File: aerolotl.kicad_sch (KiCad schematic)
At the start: 0 parts

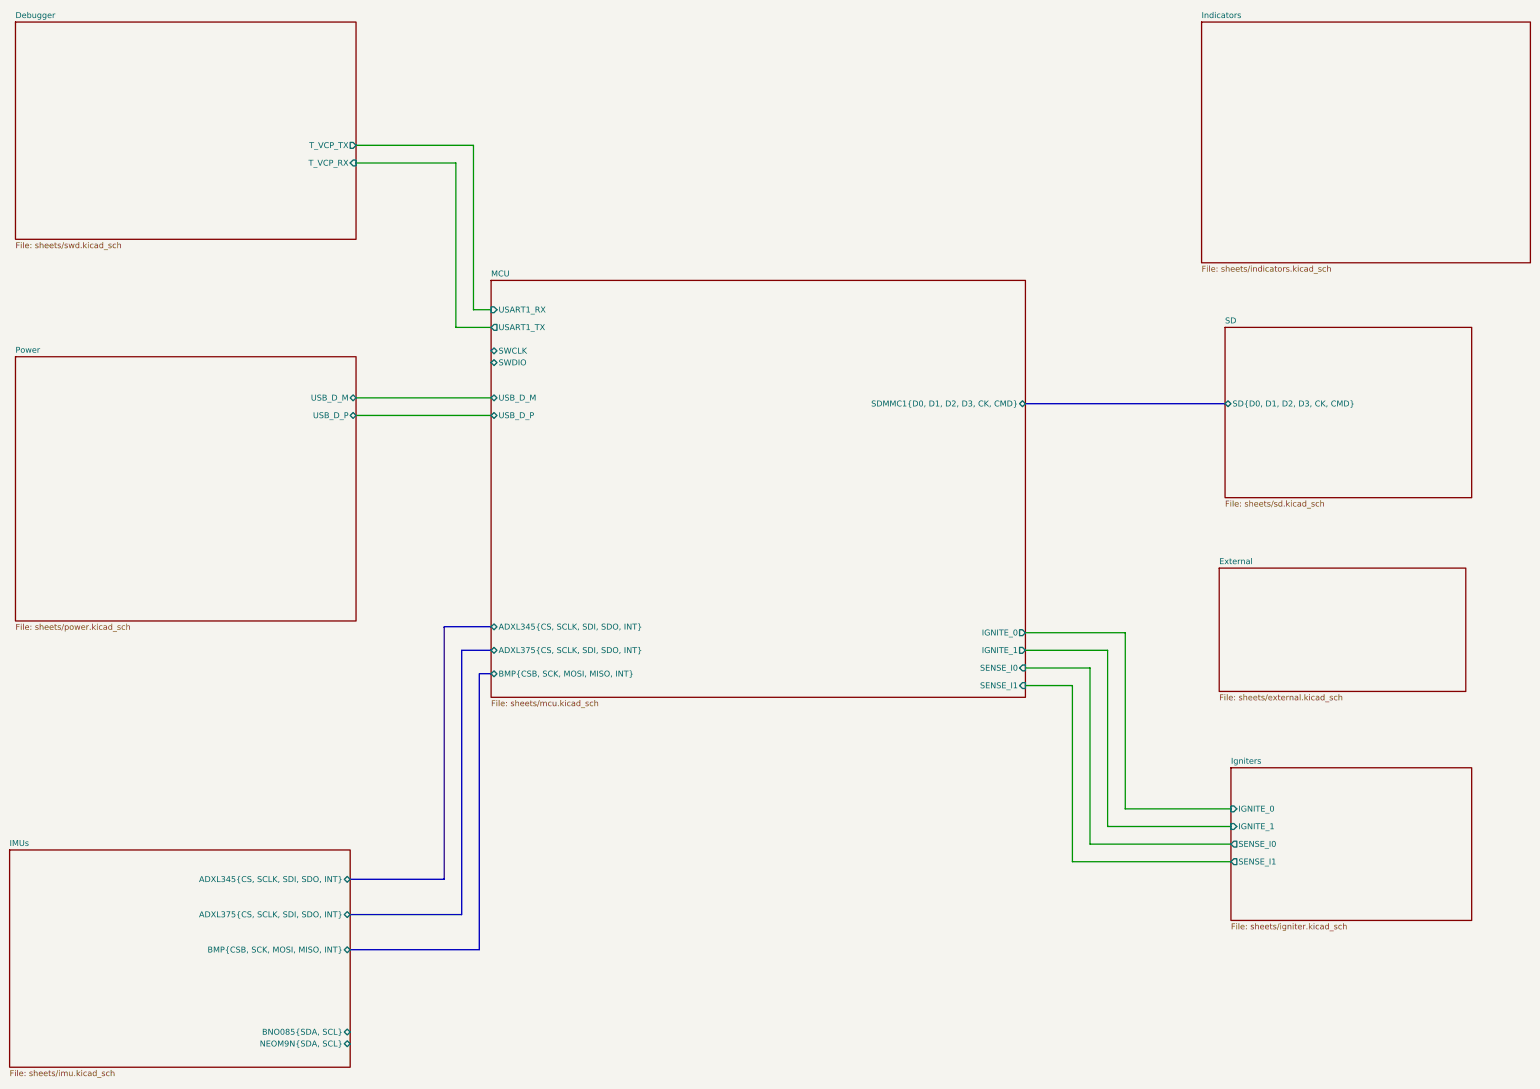
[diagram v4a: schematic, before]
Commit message: polished up circuit, added new 16.8V to 7.4V step down circuit components
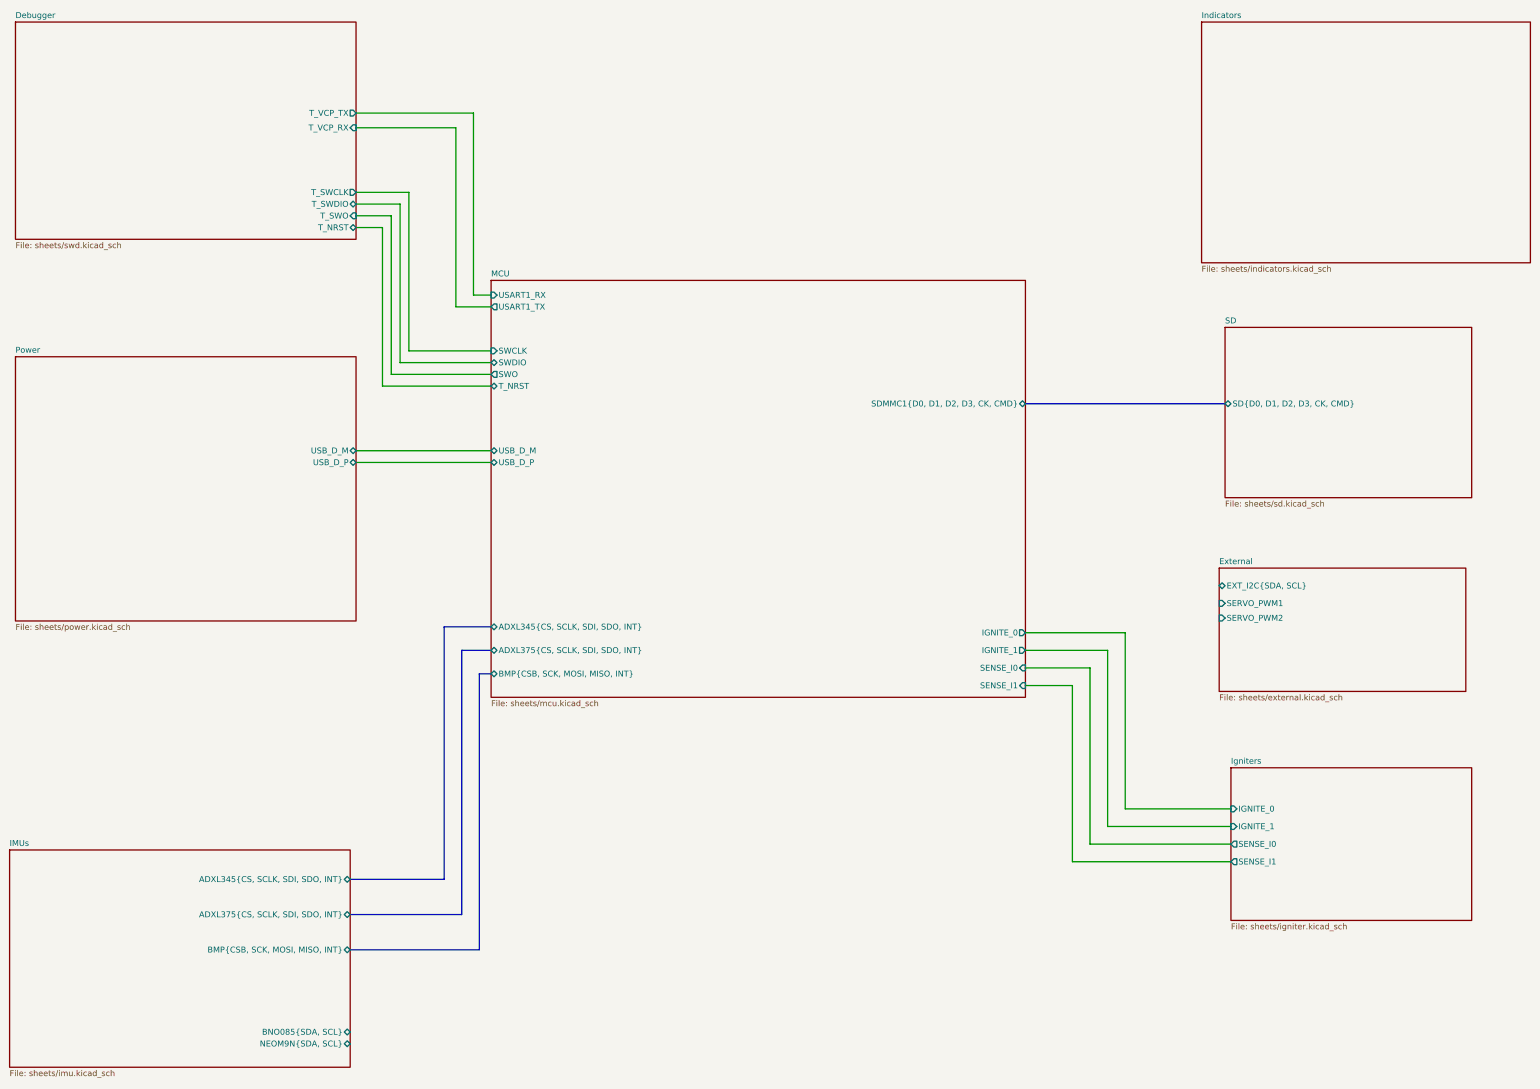
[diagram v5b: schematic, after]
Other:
- sheet Debugger ports: added T_NRST, T_SWCLK, T_SWDIO, T_SWO; removed none
- sheet External ports: added EXT_I2C{SDA, SCL}, SERVO_PWM1, SERVO_PWM2; removed none
- sheet MCU ports: added SWO, T_NRST; removed none
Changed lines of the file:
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@@
+	(wire
+		(pts
+			(xy 114.935 102.87) (xy 114.935 68.58)
+		)
+		(stroke
+			(width 0)
+			(type default)
+		)
+	)
 	(wire
 		(pts
@@
 	(wire
 		(pts
+			(xy 116.84 66.04) (xy 116.84 100.33)
+		)
+		(stroke
+			(width 0)
+			(type default)
+		)
+	)
+	(wire
+		(pts
+			(xy 105.41 71.12) (xy 113.03 71.12)
+		)
+		(stroke
+			(width 0)
+			(type default)
+		)
+	)
+	(wire
+		(pts
+			(xy 105.41 66.04) (xy 116.84 66.04)
+		)
+		(stroke
+			(width 0)
+			(type default)
+		)
+	)
+	(wire
+		(pts
 			(xy 250.19 161.29) (xy 271.78 161.29)
 		)
@@
 	(wire
 		(pts
-			(xy 105.41 59.69) (xy 127 59.69)
+			(xy 116.84 100.33) (xy 134.62 100.33)
+		)
+		(stroke
+			(width 0)
+			(type default)
+		)
+	)
+	(wire
+		(pts
+			(xy 105.41 52.07) (xy 127 52.07)
+		)
+		(stroke
+			(width 0)
+			(type default)
+		)
+	)
+	(wire
+		(pts
+			(xy 114.935 68.58) (xy 105.41 68.58)
+		)
+		(stroke
+			(width 0)
+			(type default)
+		)
+	)
+	(wire
+		(pts
+			(xy 134.62 102.87) (xy 114.935 102.87)
 		)
 		(stroke
@@
 	(wire
 		(pts
-			(xy 105.41 110.49) (xy 134.62 110.49)
+			(xy 113.03 71.12) (xy 113.03 105.41)
+		)
+		(stroke
+			(width 0)
+			(type default)
+		)
+	)
+	(wire
+		(pts
+			(xy 105.41 121.92) (xy 134.62 121.92)
 		)
 		(stroke
@@
 	(wire
 		(pts
+			(xy 113.03 105.41) (xy 134.62 105.41)
+		)
+		(stroke
+			(width 0)
+			(type default)
+		)
+	)
+	(wire
+		(pts
+			(xy 111.125 73.66) (xy 105.41 73.66)
+		)
+		(stroke
+			(width 0)
+			(type default)
+		)
+	)
+	(wire
+		(pts
+			(xy 111.125 107.95) (xy 111.125 73.66)
+		)
+		(stroke
+			(width 0)
+			(type default)
+		)
+	)
+	(wire
+		(pts
 			(xy 264.16 168.91) (xy 264.16 207.01)
 		)
@@
 	(wire
 		(pts
-			(xy 105.41 55.88) (xy 130.81 55.88)
+			(xy 105.41 48.895) (xy 130.81 48.895)
 		)
 		(stroke
@@
 	(wire
 		(pts
-			(xy 130.81 55.88) (xy 130.81 91.44)
+			(xy 130.81 48.895) (xy 130.81 88.265)
 		)
 		(stroke
@@
 	(wire
 		(pts
-			(xy 105.41 114.3) (xy 134.62 114.3)
-		)
-		(stroke
-			(width 0)
-			(type default)
-		)
-	)
-	(wire
-		(pts
-			(xy 130.81 91.44) (xy 134.62 91.44)
+			(xy 105.41 124.46) (xy 134.62 124.46)
+		)
+		(stroke
+			(width 0)
+			(type default)
+		)
+	)
+	(wire
+		(pts
+			(xy 130.81 88.265) (xy 134.62 88.265)
 		)
 		(stroke
@@
 	(wire
 		(pts
-			(xy 127 59.69) (xy 127 95.25)
-		)
-		(stroke
-			(width 0)
-			(type default)
-		)
-	)
-	(wire
-		(pts
-			(xy 127 95.25) (xy 134.62 95.25)
+			(xy 134.62 107.95) (xy 111.125 107.95)
+		)
+		(stroke
+			(width 0)
+			(type default)
+		)
+	)
+	(wire
+		(pts
+			(xy 127 52.07) (xy 127 90.805)
+		)
+		(stroke
+			(width 0)
+			(type default)
+		)
+	)
+	(wire
+		(pts
+			(xy 127 90.805) (xy 134.62 90.805)
 		)
 		(stroke
@@
 		)
 		(pin "T_VCP_RX" input
-			(at 105.41 59.69 0)
+			(at 105.41 52.07 0)
 			(effects
 				(font
@@
 		)
 		(pin "T_VCP_TX" output
-			(at 105.41 55.88 0)
+			(at 105.41 48.895 0)
+			(effects
+				(font
+					(size 1.27 1.27)
+				)
+				(justify right)
+			)
+		)
+		(pin "T_SWCLK" output
+			(at 105.41 66.04 0)
+			(effects
+				(font
+					(size 1.27 1.27)
+				)
+				(justify right)
+			)
+		)
+		(pin "T_SWDIO" bidirectional
+			(at 105.41 68.58 0)
+			(effects
+				(font
+					(size 1.27 1.27)
+				)
+				(justify right)
+			)
+		)
+		(pin "T_SWO" input
+			(at 105.41 71.12 0)
+			(effects
+				(font
+					(size 1.27 1.27)
+				)
+				(justify right)
+			)
+		)
+		(pin "T_NRST" bidirectional
+			(at 105.41 73.66 0)
 			(effects
 				(font
@@
 			)
 		)
+		(pin "EXT_I2C{SDA, SCL}" bidirectional
+			(at 292.1 151.13 180)
+			(effects
+				(font
+					(size 1.27 1.27)
+				)
+				(justify left)
+			)
+		)
+		(pin "SERVO_PWM1" input
+			(at 292.1 154.94 180)
+			(effects
+				(font
+					(size 1.27 1.27)
+				)
+				(justify left)
+			)
+		)
+		(pin "SERVO_PWM2" input
+			(at 292.1 158.115 180)
+			(effects
+				(font
+					(size 1.27 1.27)
+				)
+				(justify left)
+			)
+		)
 		(instances
 			(project "aerolotl"
@@
 		)
 		(pin "USB_D_M" bidirectional
-			(at 105.41 110.49 0)
+			(at 105.41 121.92 0)
 			(effects
 				(font
@@
 		)
 		(pin "USB_D_P" bidirectional
-			(at 105.41 114.3 0)
+			(at 105.41 124.46 0)
 			(effects
 				(font
@@
 		)
 		(pin "USART1_RX" input
-			(at 134.62 91.44 180)
+			(at 134.62 88.265 180)
 			(effects
 				(font
@@
 		)
 		(pin "USART1_TX" output
-			(at 134.62 95.25 180)
+			(at 134.62 90.805 180)
 			(effects
 				(font
@@
 			)
 		)
-		(pin "SWCLK" bidirectional
-			(at 134.62 100.33 180)
-			(effects
-				(font
-					(size 1.27 1.27)
-				)
-				(justify left)
-			)
-		)
 		(pin "SWDIO" bidirectional
 			(at 134.62 102.87 180)
@@
 		)
 		(pin "USB_D_M" bidirectional
-			(at 134.62 110.49 180)
+			(at 134.62 121.92 180)
 			(effects
 				(font
@@
 		)
 		(pin "USB_D_P" bidirectional
-			(at 134.62 114.3 180)
+			(at 134.62 124.46 180)
 			(effects
 				(font
@@
 			(effects
 				(font
+					(size 1.27 1.27)
+				)
+				(justify left)
+			)
+		)
+		(pin "SWCLK" input
+			(at 134.62 100.33 180)
+			(effects
+				(font
+					(size 1.27 1.27)
+				)
+				(justify left)
+			)
+		)
+		(pin "SWO" output
+			(at 134.62 105.41 180)
+			(effects
+				(font
+					(size 1.27 1.27)
+				)
+				(justify left)
+			)
+		)
+		(pin "T_NRST" bidirectional
+			(at 134.62 107.95 180)
+			(effects
+				(font

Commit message: second push
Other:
- sheet IMUs renamed Sensors
- sheet MCU ports: added NEOM9N_EXTI0, NEOM9N_RST, USART2_RX, USART2_TX; removed none
- sheet Sensors: file sheets/imu.kicad_sch -> sheets/sensors.kicad_sch
- sheet Sensors ports: added NEOM9N{TX, RX, PPS, RST}; removed NEOM9N{SDA, SCL}
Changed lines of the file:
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@@
 	(generator_version "9.0")
 	(paper "A3")
+	(bus_entry
+		(at 204.47 193.675)
+		(size 2.54 -2.54)
+		(stroke
+			(width 0)
+			(type default)
+		)
+	)
+	(bus_entry
+		(at 190.5 193.675)
+		(size 2.54 -2.54)
+		(stroke
+			(width 0)
+			(type default)
+		)
+	)
+	(bus_entry
+		(at 200.025 193.675)
+		(size 2.54 -2.54)
+		(stroke
+			(width 0)
+			(type default)
+		)
+	)
+	(bus_entry
+		(at 194.945 193.675)
+		(size 2.54 -2.54)
+		(stroke
+			(width 0)
+			(type default)
+		)
+	)
+	(bus
+		(pts
+			(xy 194.945 193.675) (xy 200.025 193.675)
+		)
+		(stroke
+			(width 0)
+			(type default)
+		)
+	)
 	(wire
 		(pts
@@
 		)
 	)
+	(bus
+		(pts
+			(xy 189.865 247.015) (xy 104.14 247.015)
+		)
+		(stroke
+			(width 0)
+			(type default)
+		)
+	)
 	(wire
 		(pts
@@
 		)
 	)
+	(bus
+		(pts
+			(xy 190.5 193.675) (xy 194.945 193.675)
+		)
+		(stroke
+			(width 0)
+			(type default)
+		)
+	)
 	(wire
 		(pts
@@
 		)
 	)
+	(bus
+		(pts
+			(xy 189.865 247.015) (xy 189.865 193.675)
+		)
+		(stroke
+			(width 0)
+			(type default)
+		)
+	)
 	(wire
 		(pts
@@
 	(wire
 		(pts
+			(xy 197.485 175.26) (xy 197.485 191.135)
+		)
+		(stroke
+			(width 0)
+			(type default)
+		)
+	)
+	(wire
+		(pts
 			(xy 260.35 210.82) (xy 294.64 210.82)
 		)
@@
 		)
 	)
+	(bus
+		(pts
+			(xy 200.025 193.675) (xy 204.47 193.675)
+		)
+		(stroke
+			(width 0)
+			(type default)
+		)
+	)
 	(wire
 		(pts
@@
 	(bus
 		(pts
+			(xy 189.865 193.675) (xy 190.5 193.675)
+		)
+		(stroke
+			(width 0)
+			(type default)
+		)
+	)
+	(bus
+		(pts
 			(xy 124.46 160.02) (xy 134.62 160.02)
 		)
@@
 	(wire
 		(pts
+			(xy 207.01 175.26) (xy 207.01 191.135)
+		)
+		(stroke
+			(width 0)
+			(type default)
+		)
+	)
+	(wire
+		(pts
 			(xy 250.19 165.1) (xy 267.97 165.1)
 		)
@@
 	(wire
 		(pts
+			(xy 193.04 175.26) (xy 193.04 191.135)
+		)
+		(stroke
+			(width 0)
+			(type default)
+		)
+	)
+	(wire
+		(pts
 			(xy 130.81 48.895) (xy 130.81 88.265)
 		)
@@
 		)
 	)
+	(wire
+		(pts
+			(xy 202.565 175.26) (xy 202.565 191.135)
+		)
+		(stroke
+			(width 0)
+			(type default)
+		)
+	)
 	(bus
 		(pts
@@
 			(width 0)
 			(type default)
+		)
+	)
+	(label "NEOM9N.PPS"
+		(at 202.565 191.135 90)
+		(effects
+			(font
+				(size 1.27 1.27)
+			)
+			(justify left bottom)
+		)
+	)
+	(label "NEOM9N.RST"
+		(at 207.01 191.135 90)
+		(effects
+			(font
+				(size 1.27 1.27)
+			)
+			(justify left bottom)
+		)
+	)
+	(label "NEOM9N.RX"
+		(at 197.485 189.23 90)
+		(effects
+			(font
+				(size 1.27 1.27)
+			)
+			(justify left bottom)
+		)
+	)
+	(label "NEOM9N.RX"
+		(at 193.04 189.23 90)
+		(effects
+			(font
+				(size 1.27 1.27)
+			)
+			(justify left bottom)
 		)
 	)
@@
 			(color 0 0 0 0.0000)
 		)
-		(property "Sheetname" "IMUs"
+		(property "Sheetname" "Sensors"
 			(at 30.48 207.5684 0)
 			(effects
@@
 			)
 		)
-		(property "Sheetfile" "sheets/imu.kicad_sch"
+		(property "Sheetfile" "sheets/sensors.kicad_sch"
 			(at 30.48 255.8546 0)
 			(effects
@@
 		)
 		(pin "BNO085{SDA, SCL}" bidirectional
-			(at 104.14 247.65 0)
-			(effects
-				(font
-					(size 1.27 1.27)
-				)
-				(justify right)
-			)
-		)
-		(pin "NEOM9N{SDA, SCL}" bidirectional
-			(at 104.14 250.19 0)
+			(at 104.14 239.395 0)
 			(effects
 				(font
@@
 		(pin "BMP{CSB, SCK, MOSI, MISO, INT}" bidirectional
 			(at 104.14 229.87 0)
+			(effects
+				(font
+					(size 1.27 1.27)
+				)
+				(justify right)
+			)
+		)
+		(pin "NEOM9N{TX, RX, PPS, RST}" bidirectional
+			(at 104.14 247.015 0)
 			(effects
 				(font
@@
 			(effects
 				(font
+					(size 1.27 1.27)
+				)
+				(justify left)
+			)
+		)
+		(pin "NEOM9N_EXTI0" input
+			(at 202.565 175.26 270)
+			(effects
+				(font
+					(size 1.27 1.27)
+				)
+				(justify left)
+			)
+		)
+		(pin "NEOM9N_RST" output
+			(at 207.01 175.26 270)
+			(effects
+				(font
+					(size 1.27 1.27)
+				)
+				(justify left)
+			)
+		)
+		(pin "USART2_RX" input
+			(at 197.485 175.26 270)
+			(effects
+				(font
+					(size 1.27 1.27)
+				)
+				(justify left)
+			)
+		)
+		(pin "USART2_TX" output
+			(at 193.04 175.26 270)
+			(effects
+				(font

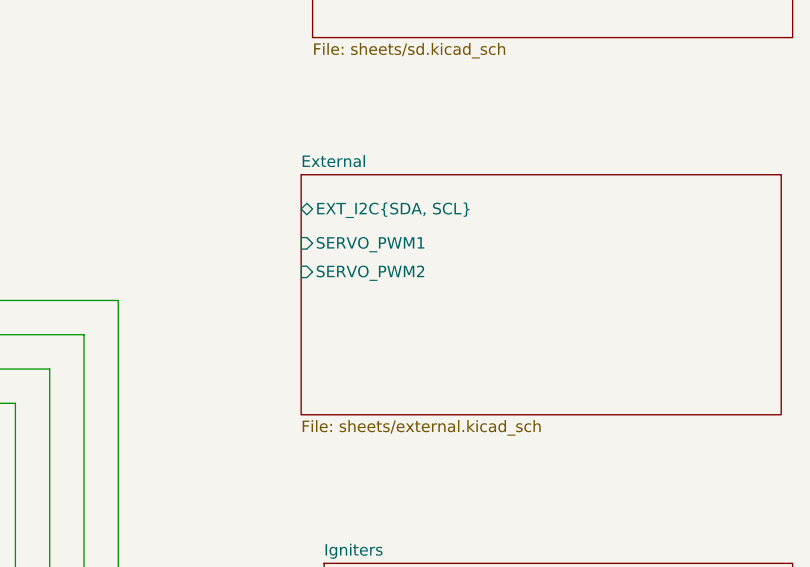
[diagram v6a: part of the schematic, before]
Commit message: Added pinouts for I2C
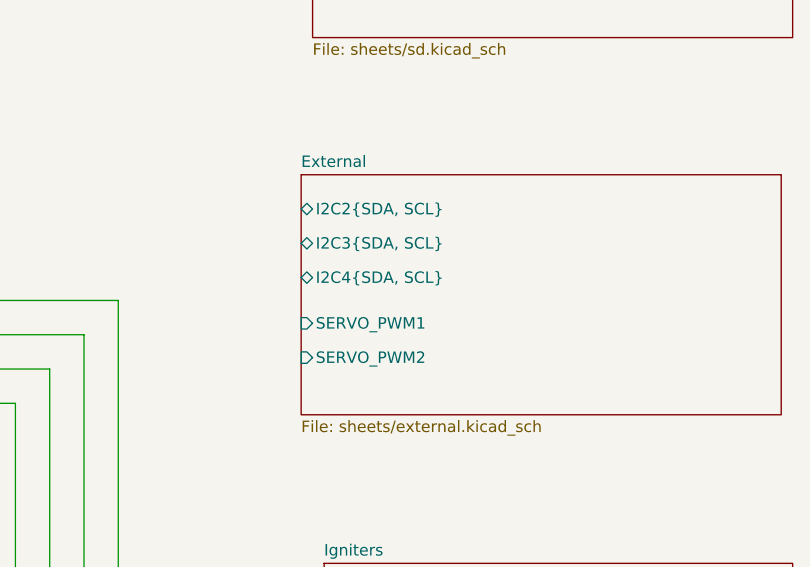
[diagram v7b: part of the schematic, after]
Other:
- sheet External ports: added I2C2{SDA, SCL}, I2C3{SDA, SCL}, I2C4{SDA, SCL}; removed EXT_I2C{SDA, SCL}
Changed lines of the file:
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@@
 			)
 		)
-		(pin "EXT_I2C{SDA, SCL}" bidirectional
+		(pin "SERVO_PWM1" input
+			(at 292.1 163.83 180)
+			(effects
+				(font
+					(size 1.27 1.27)
+				)
+				(justify left)
+			)
+		)
+		(pin "SERVO_PWM2" input
+			(at 292.1 167.64 180)
+			(effects
+				(font
+					(size 1.27 1.27)
+				)
+				(justify left)
+			)
+		)
+		(pin "I2C2{SDA, SCL}" bidirectional
 			(at 292.1 151.13 180)
 			(effects
@@
 			)
 		)
-		(pin "SERVO_PWM1" input
+		(pin "I2C3{SDA, SCL}" bidirectional
 			(at 292.1 154.94 180)
 			(effects
@@
 			)
 		)
-		(pin "SERVO_PWM2" input
-			(at 292.1 158.115 180)
+		(pin "I2C4{SDA, SCL}" bidirectional
+			(at 292.1 158.75 180)
 			(effects
 				(font
